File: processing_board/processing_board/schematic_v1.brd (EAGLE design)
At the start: 65 x 70 mm, 46 parts, among them Q1 BSS138, Q2 BSS138, Q3 BSS138, Q4 BSS138

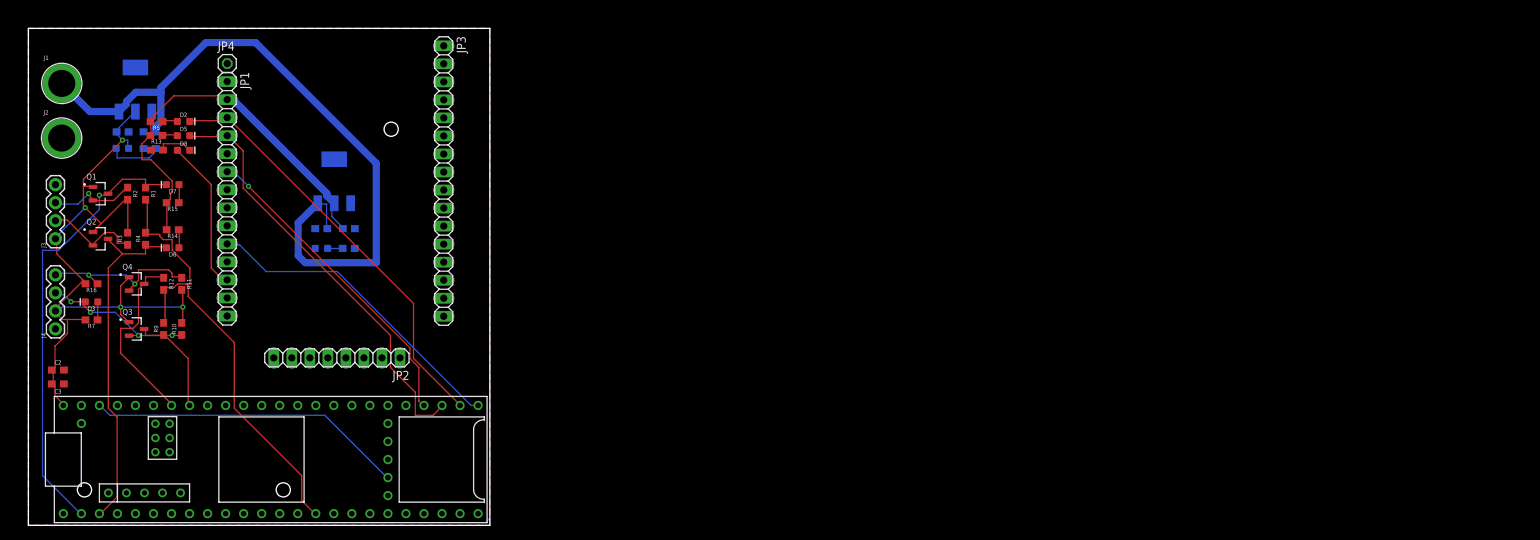
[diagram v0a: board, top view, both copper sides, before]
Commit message: new teensy 4.1 footprint
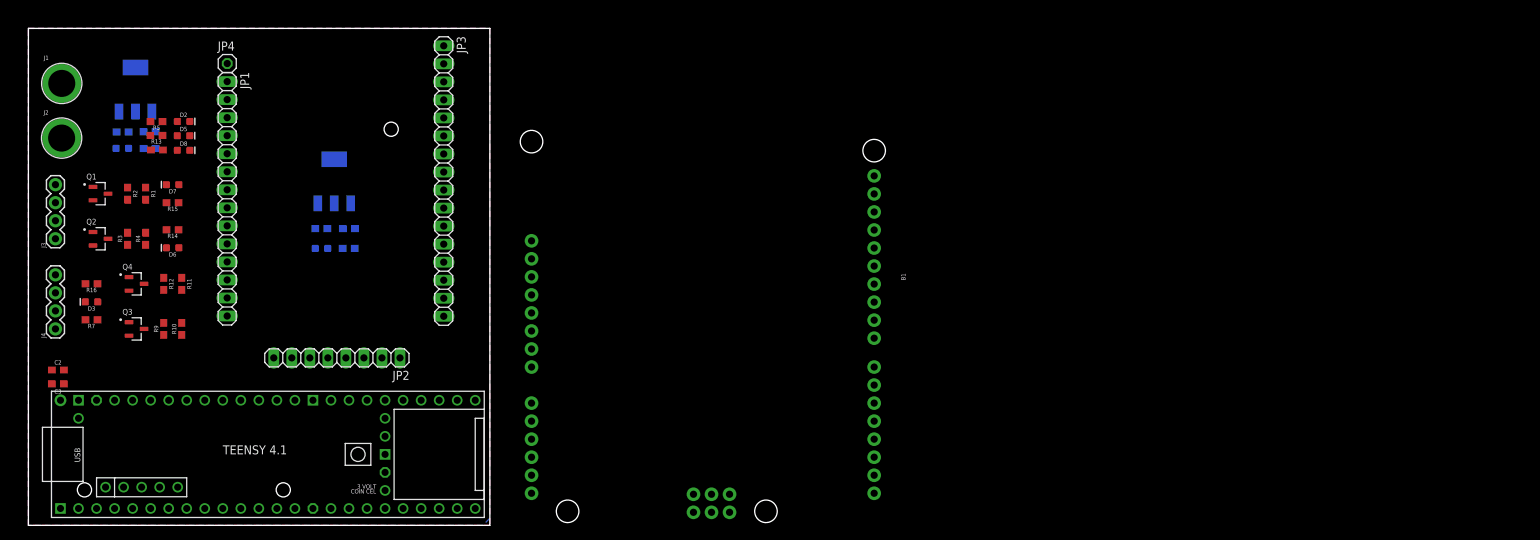
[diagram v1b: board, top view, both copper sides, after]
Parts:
- removed U$1: DEV-16771, teensy_4_1:DEV-16771
- added B1: ARDUINO_UNO_R3, SparkFun-Boards:ARDUINO_R3
- added U$4: TEENSY41-E, teensy:TENNSY41-E
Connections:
- removed net 3.3V: U$1.3.3V@1, U$1.3.3V@2
- removed net 5V: U$1.5V
- removed net G: U$1.G
- removed net N$9: JP1.10, U$1.D33
- removed net USB_GND1: U$1.USB_GND
- removed net USB_GND2: U$1.USB_GND@2
- removed net VBAT: U$1.VBAT
- removed net VUSB: U$1.VUSB
- new net N$15: U$4.37-PWM
- net +5V: now also U$4.VIN; no longer U$1.VIN
- net GND: now also U$4.+5V, U$4.GND1, U$4.GND2, U$4.GND3, U$4.GND4, U$4.GND5, U$4.GND6; no longer U$1.AGND, U$1.GND, U$1.GND@1, U$1.GND@2
- net N$1: now also U$4.35-TX8; no longer U$1.D35
- net N$11: now also U$4.1-TX1/MISO1/CTX2; no longer U$1.D1
- net N$2: now also U$4.34-RX8; no longer U$1.D34
- net N$5: now also U$4.0-RX1/CS1/CRX2; no longer U$1.D0
- net RESET_: now also JP1.10, U$4.33-MCLK2; no longer U$1.D36
- net SCL: now also U$4.16-A2/RX4/SCL1; no longer U$1.D20/A6
- net SDA: now also U$4.17-A3/TX4/SDA1; no longer U$1.D19/A5
- net TEENSY_3.3V: no longer U$1.3.3V
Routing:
- net +5V: track 105.7 -> 0.00 mm, vias 4 -> 0
- net +15V: track 105.4 -> 0.00 mm
- net TEENSY_3.3V: track 65.4 -> 0.00 mm
- net N$5: track 63.6 -> 0.00 mm, vias 1 -> 0
- net N$1: track 60.5 -> 0.00 mm
- net N$2: track 60.0 -> 0.00 mm
- net +3.3V: track 58.5 -> 0.00 mm
- net N$11: track 49.8 -> 0.00 mm
- net RESET_: track 45.0 -> 0.00 mm, vias 1 -> 0
- net N$9: track 44.9 -> 0.00 mm
- net 3.3V: track 44.8 -> 0.00 mm
- net SCL: track 26.2 -> 0.00 mm
- net CAN_TX1: track 24.0 -> 0.00 mm, vias 2 -> 0
- net CAN_RX1: track 22.4 -> 0.00 mm, vias 4 -> 0
- net N$3: track 21.6 -> 0.00 mm
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
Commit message: pushing
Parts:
- added J5: (no value), SparkFun-Connectors:1X02
- added R18: 10k, SparkFun-Resistors:0603
- added R19: 8.2k, SparkFun-Resistors:0603
- moved B1 2.24 mm to (93.0, 36.0)
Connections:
- new net POWER_DIVIDED: R18.1, R19.2, U$4.27-A13/SCK1
- net +15V: now also R18.2
- net +5V: now also B1.VIN
- net CAN_RX1: now also J5.1
- net CAN_TX1: now also J5.2
- net GND: now also B1.GND@1, R19.1
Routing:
- removed copper zone on layer 16, net GND
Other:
- board size 65 x 70 mm -> 120 x 70 mm

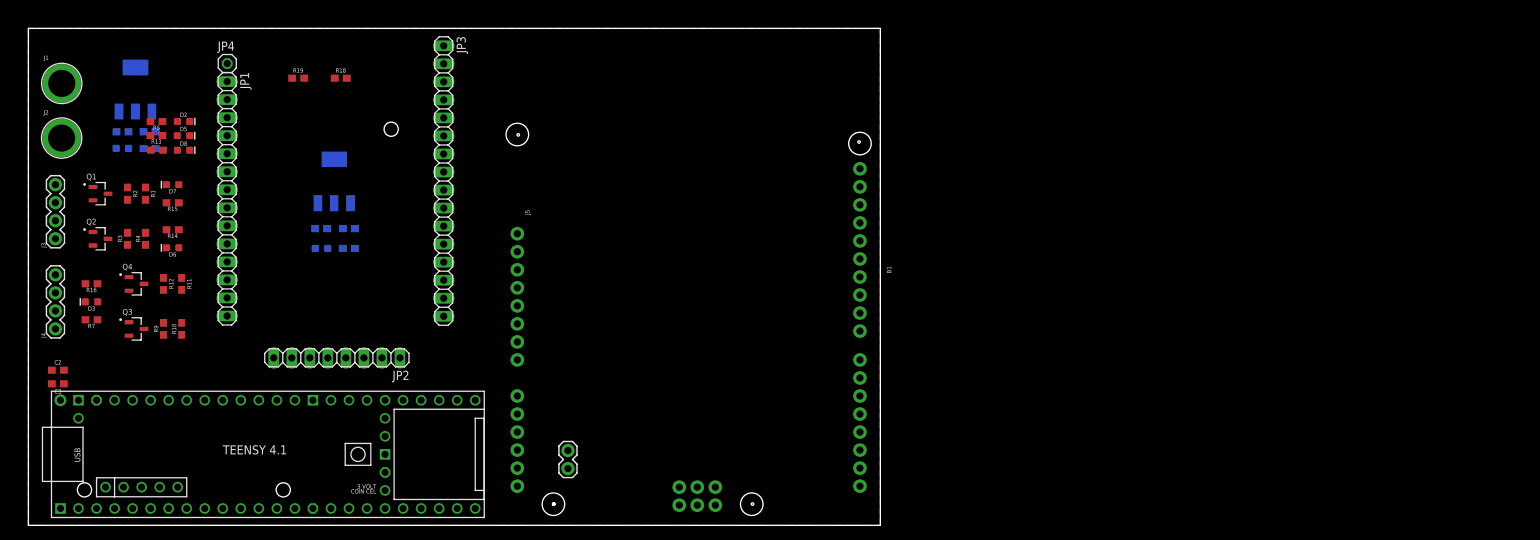
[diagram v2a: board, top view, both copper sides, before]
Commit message: added arduino headers
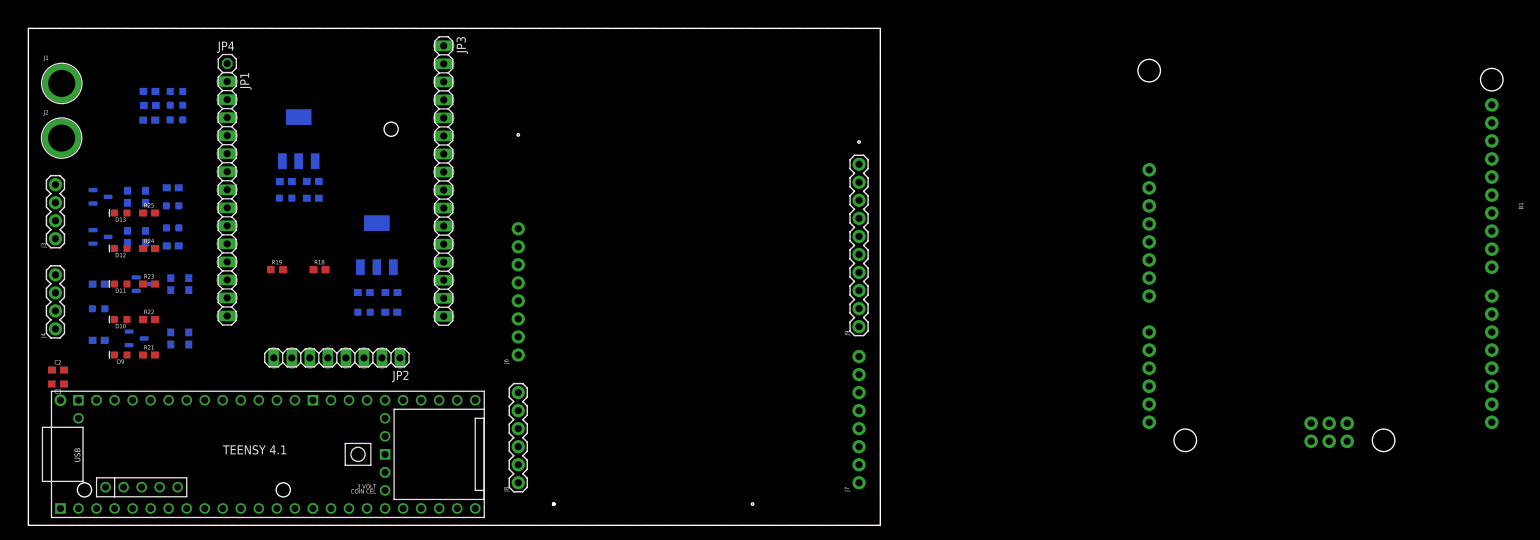
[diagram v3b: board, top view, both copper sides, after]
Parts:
- removed J5: (no value), SparkFun-Connectors:1X02
- added D10, D11, D12, D13, D9: GREEN, SparkFun-LED:LED-0603
- added J6, J7: (no value), SparkFun-Connectors:1X08_NO_SILK
- added J8: (no value), SparkFun-Connectors:1X06
- added J9: (no value), SparkFun-Connectors:1X10
- added R21, R22, R23, R24, R25: 10k, SparkFun-Resistors:0603
- moved B1 89.5 mm to (182.0, 45.0)
- moved R18 27.2 mm to (41.0, 36.0)
- moved R19 27.2 mm to (35.0, 36.0)
- moved C1 24.0 mm to (36.3, 48.4)
- moved C4 24.0 mm to (40.1, 48.4)
- moved R6 24.0 mm to (40.1, 46.1)
- moved U$2 24.0 mm to (38.1, 54.4)
- moved D1 24.0 mm to (36.2, 46.1)
- moved C5 10.8 mm to (51.1, 32.8)
- moved C6 10.8 mm to (47.2, 32.8)
- moved U$3 10.8 mm to (49.1, 39.5)
- moved D4 10.8 mm to (47.3, 30.0)
- moved R8 10.8 mm to (51.1, 30.0)
- moved D8 6.42 mm to (20.9, 59.2), flipped to the bottom, turned to 180 degrees
- moved R17 6.34 mm to (17.1, 59.1), flipped to the bottom, turned to 180 degrees
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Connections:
- new net N$16: D9.A, R21.1
- new net N$17: D10.C
- new net N$18: D10.A, R22.1
- new net N$20: D11.A, R23.1
- new net N$21: D12.C
- new net N$22: D12.A, R24.1
- new net N$24: D13.A, R25.1
- new net STATUS1: R21.2, U$4.2-OUT2
- new net STATUS2: R22.2, U$4.3-LRCLK2
- new net STATUS3: R23.2, U$4.4-BCLK2
- new net STATUS4: R24.2, U$4.5-IN2
- new net STATUS5: R25.2, U$4.6-OUT1D
- net CAN_RX1: no longer J5.1
- net CAN_TX1: no longer J5.2
- net GND: now also D11.C, D13.C, D9.C

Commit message: added arduino pins
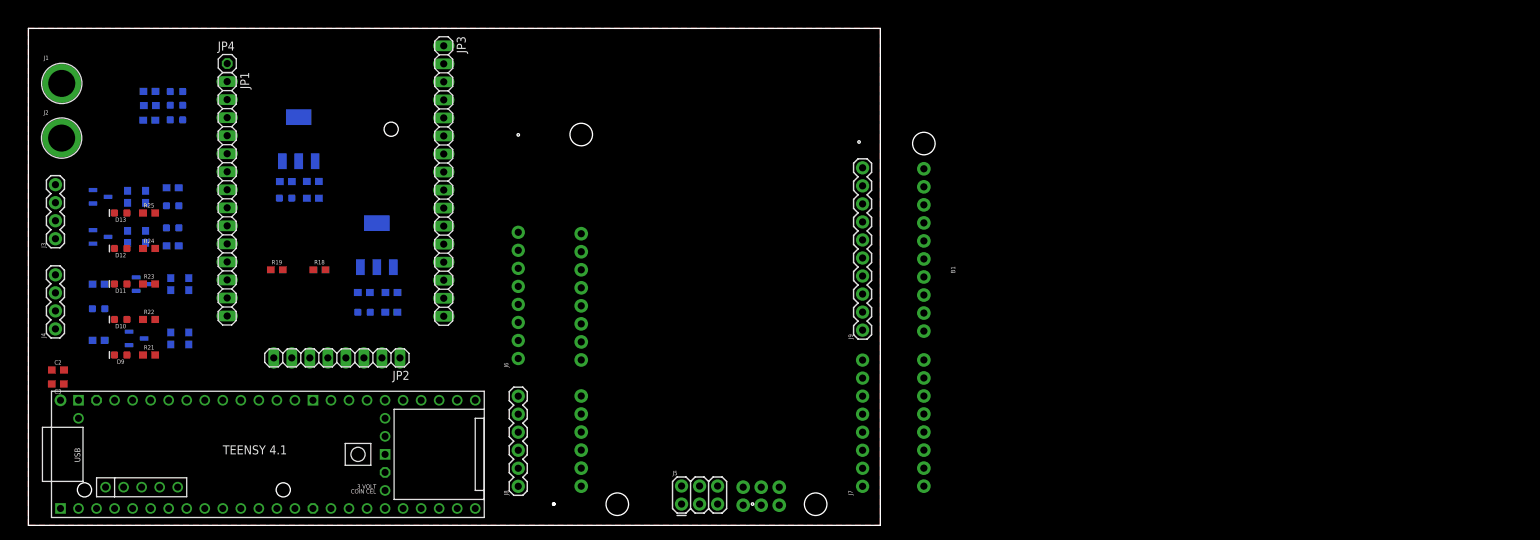
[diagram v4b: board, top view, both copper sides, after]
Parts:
- added J5: FEMALE 2x3, SparkFun-Connectors:2X3
- moved B1 80.5 mm to (102.0, 36.0)
- moved J7 0.71 mm to (117.5, 5.50)
- moved J9 0.71 mm to (117.5, 27.5)
- moved J6 0.50 mm to (69.0, 23.5)
- moved J8 0.50 mm to (69.0, 5.50)
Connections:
- net +5V: now also J6.1
- net GND: now also J6.2, J6.3

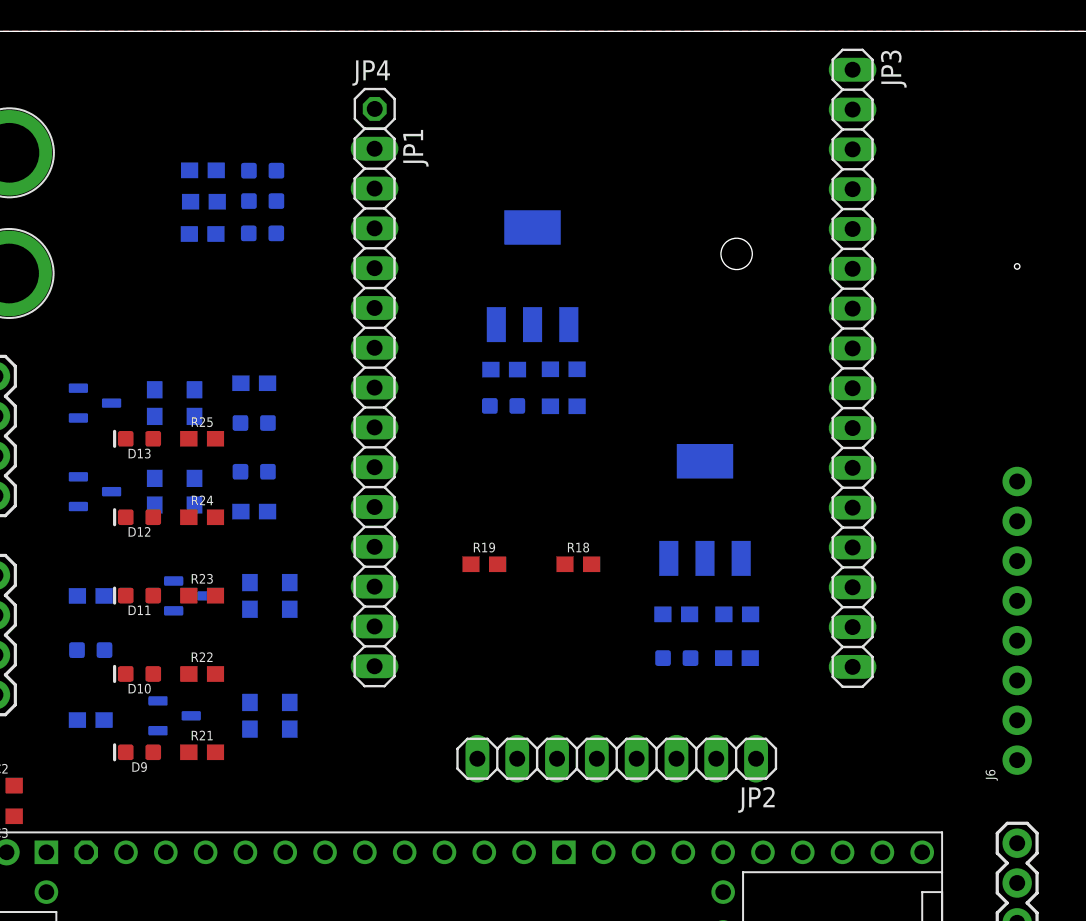
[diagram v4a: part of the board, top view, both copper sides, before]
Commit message: added dip switch
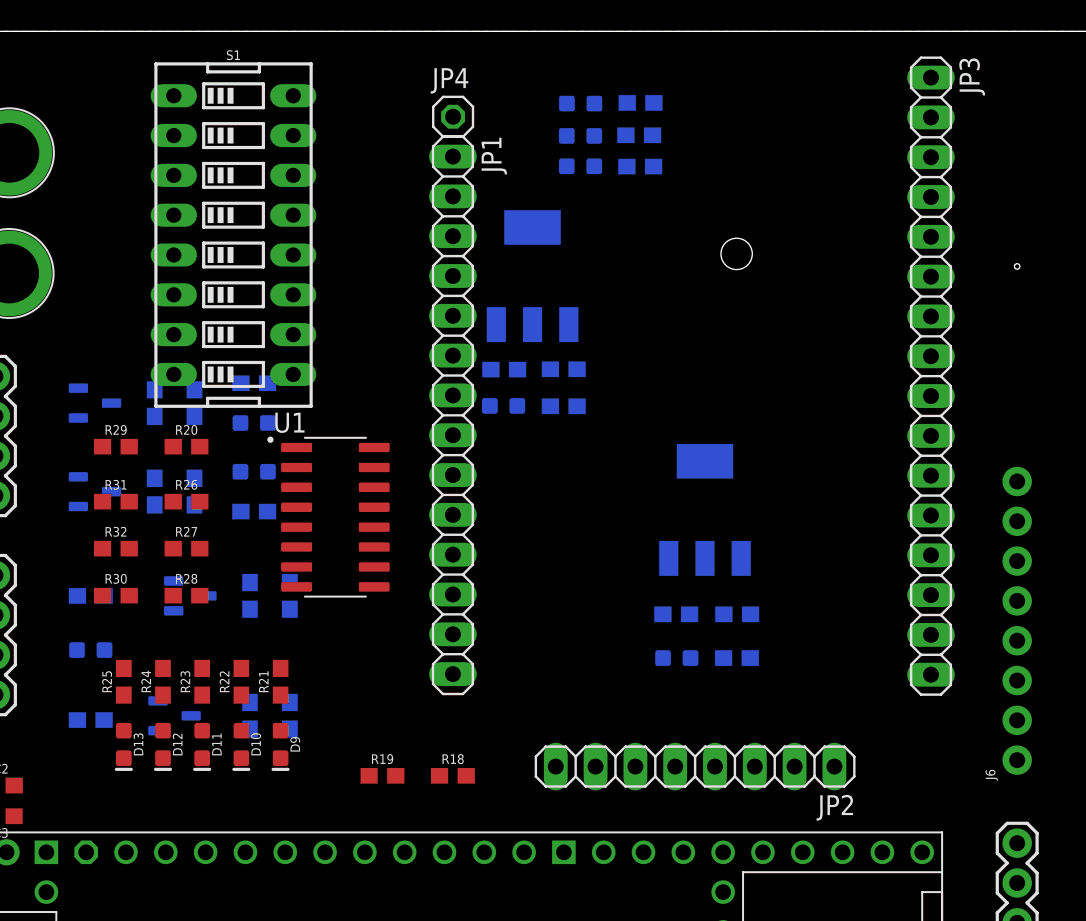
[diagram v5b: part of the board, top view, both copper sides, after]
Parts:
- added R20, R26, R27, R28, R29, R30, R31, R32: 10k, SparkFun-Resistors:0603
- added S1: (no value), SparkFun-Switches:DIPSWITCH-08
- added U1: SN74ALS166D, SN74ALS166D - TI level shifter:SOIC127P600X175-16N
- moved R13 29.2 mm to (45.0, 65.4), turned to 180 degrees
- moved R17 28.1 mm to (44.9, 63.4), turned to 0 degrees
- moved R5 27.9 mm to (45.0, 61.4), turned to 180 degrees
- moved D5 21.9 mm to (41.1, 65.4), turned to 0 degrees
- moved D8 20.7 mm to (41.1, 63.3), turned to 0 degrees
- moved D2 20.3 mm to (41.1, 61.4), turned to 0 degrees
- moved D13 19.5 mm to (12.0, 24.5), turned to 270 degrees
- moved R25 16.3 mm to (12.0, 28.5), turned to 90 degrees
- moved R18 15.7 mm to (33.0, 22.5)
- moved R19 15.0 mm to (28.5, 22.5)
- moved D12 14.6 mm to (14.5, 24.5), turned to 270 degrees
- moved R24 10.8 mm to (14.5, 28.5), turned to 90 degrees
- moved D11 10.3 mm to (17.0, 24.5), turned to 270 degrees
- moved D9 9.01 mm to (22.0, 24.5), turned to 270 degrees
- moved D10 7.91 mm to (19.5, 24.5), turned to 270 degrees
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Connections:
- new net 3P3_1: S1.10, S1.11, S1.12, S1.13, S1.14, S1.15, S1.16, S1.9, U$4.3V3-3
- new net A: R20.2, S1.1, U1.2
- new net C: R27.2, S1.3, U1.4
- new net D: R28.2, S1.4, U1.5
- new net DIP_SW_SERIAL: U$4.41-A17/MISO1, U1.13
- new net E: R32.2, S1.5, U1.10
- new net H: R29.2, S1.8, U1.14
- new net LS_CK: U$4.40-A16/CS1, U1.6
- new net N$23: R20.1, R26.1, R27.1, R28.1, R29.1, R30.1, R31.1, R32.1, U1.9
- new net N$25: R31.2, S1.6, U1.11
- new net N$30: R26.2, S1.2, U1.3
- new net N$9: R30.2, S1.7, U1.12
- net +5V: now also U1.16
- net GND: now also U1.1, U1.15, U1.7, U1.8

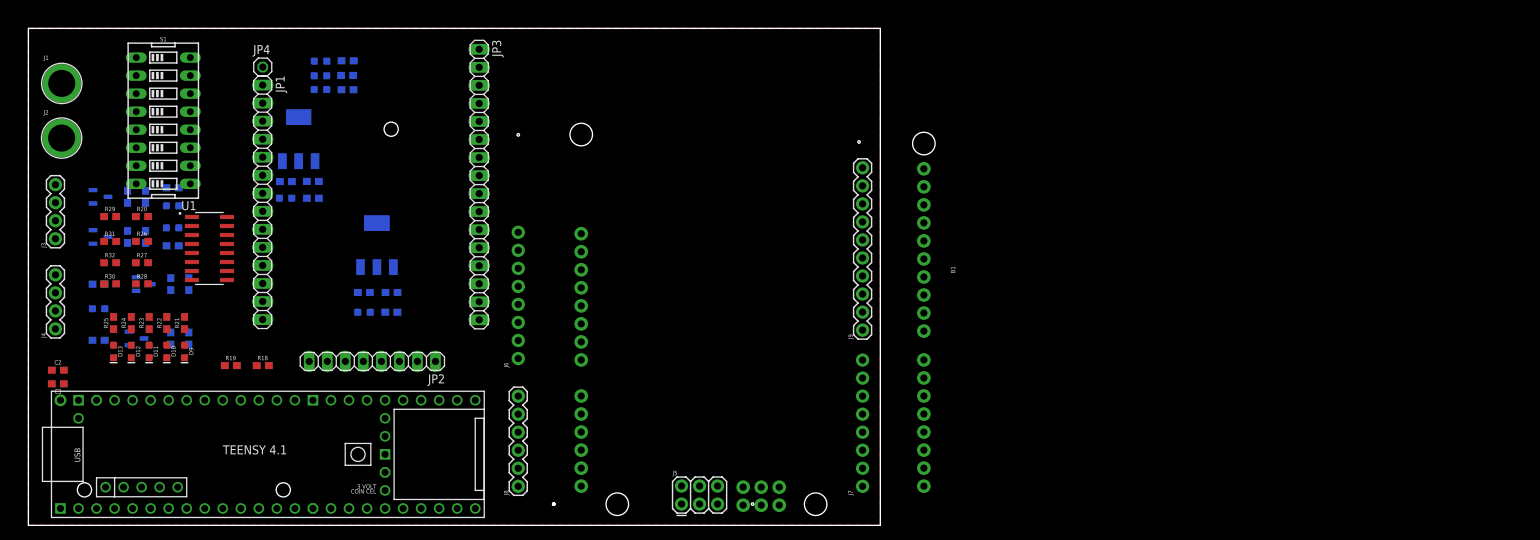
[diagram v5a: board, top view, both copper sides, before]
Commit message: fixed dip sw
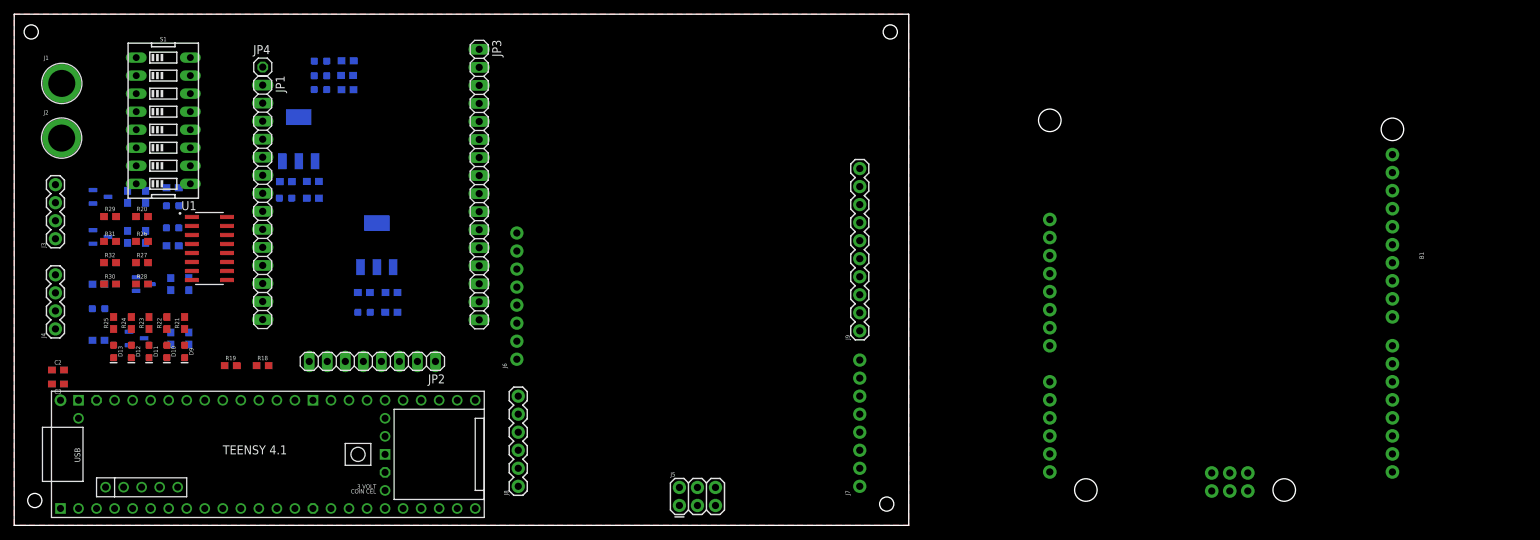
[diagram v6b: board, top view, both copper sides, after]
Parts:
- moved B1 66.0 mm to (168.0, 38.0)
- moved J9 0.41 mm to (117.1, 27.4)
- moved J7 0.40 mm to (117.1, 5.50)
- moved J5 0.36 mm to (91.7, 2.80)
- moved J6 0.22 mm to (68.8, 23.4)
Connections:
- new net SH_LD: U$4.39-A15/CS/OUT1A, U1.15
- net +5V: now also U1.9
- net GND: now also R28.1; no longer U1.15
- net N$23: no longer R28.1, U1.9
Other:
- board size 120 x 70 mm -> 126 x 72 mm
